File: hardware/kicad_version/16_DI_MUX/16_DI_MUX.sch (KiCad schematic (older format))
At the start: 39 parts, among them P1 CONN_2, P2 CONN_2, P3 CONN_2, P4 CONN_2, U1 74LS165

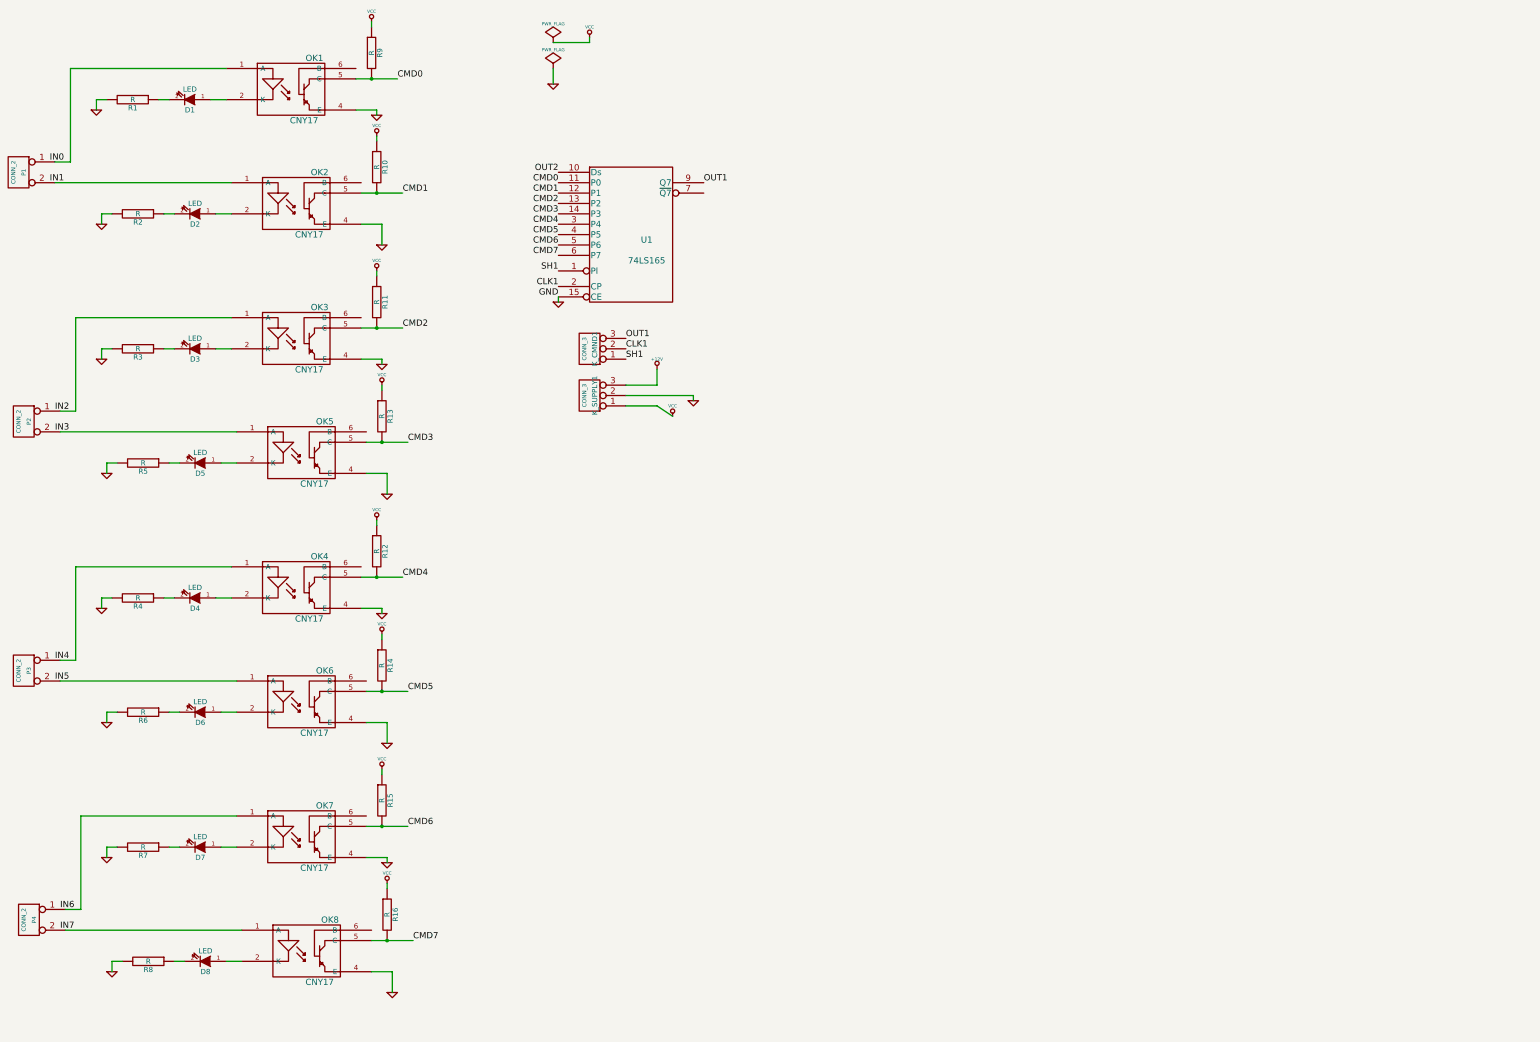
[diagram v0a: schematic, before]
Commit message: ajout de 8 entr?es correction Vcc -> 5V ajout footprint molex 2 vertical
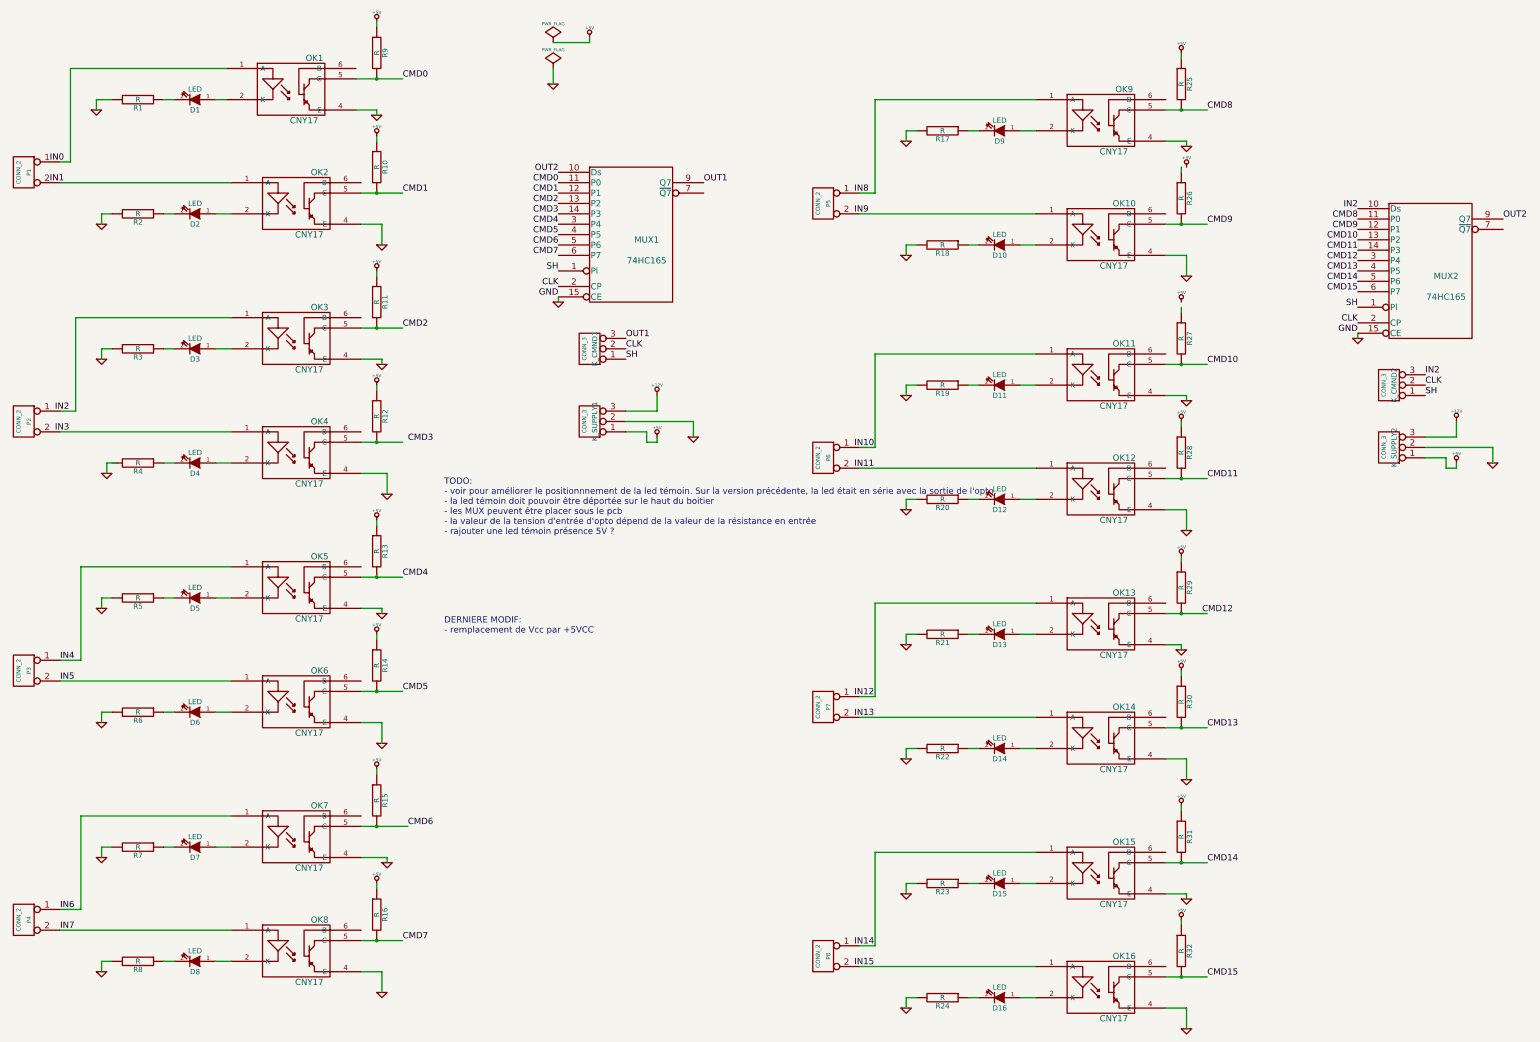
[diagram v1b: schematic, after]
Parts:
- added D10, D11, D12, D13, D14, D15, D16, D9: LED, symbol LED
- added K_CMND2, K_SUPPLY2: CONN_3, symbol CONN_3
- added MUX2: 74HC165, symbol 74LS165
- added OK10, OK11, OK12, OK13, OK14, OK15, OK16, OK9: CNY17, symbol OPTO-TRANSISTOR
- added P5, P6, P7, P8: CONN_2, symbol CONN_2
- added R17, R18, R19, R20, R21, R22, R23, R24, R25, R26, R27, R28, R29, R30, R31, R32: R, symbol R
- MUX1: renamed from U1; value 74LS165 -> 74HC165
- renumbered D5 to D4, D4 to D5, OK5 to OK4, OK4 to OK5, R13 to R12, R12 to R13, R5 to R4, R4 to R5
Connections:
- net +12V: now also K_SUPPLY2.3 (P3)
- net CMD3: no longer OK4.5 (C), R12.2
- net GND: now also K_SUPPLY2.2 (PM), MUX2.15 (CE), MUX2.8 (GND), OK10.4 (E), OK11.4 (E), OK12.4 (E), OK13.4 (E), OK14.4 (E), OK15.4 (E), OK16.4 (E), OK9.4 (E), R17.2, R18.2, R19.2, R20.2, R21.2, R22.2, R23.2, R24.2; no longer R4.2
- net IN2: now also K_CMND2.3 (P3), MUX2.10 (Ds)
- net IN4: now also OK5.1 (A), P3.1 (P1)
- net IN5: now also OK6.1 (A), P3.2 (PM)
- net IN6: now also OK7.1 (A), P4.1 (P1)
- net IN7: now also OK8.1 (A), P4.2 (PM)
- net OUT2: now also MUX2.9 (Q7)
- net VCC: now also MUX2.16 (VCC); no longer K_SUPPLY1.1 (P1), R10.1, R11.1, R12.1, R13.1, R14.1, R15.1, R16.1, R9.1
- net CLK1 renamed CLK
- net CLK: now also K_CMND2.2 (PM), MUX2.2 (CP)
- net SH1 renamed SH
- net SH: now also K_CMND2.1 (P1), MUX2.1 (Pl)
- new net: OK4.5 (C), R12.2
- new net: OK13.1 (A), P7.1 (P1)
- new net: D13.1 (A), OK13.2 (K)
- new net: D13.2 (K), R21.1
- new net: OK14.1 (A), P7.2 (PM)
- new net: D14.1 (A), OK14.2 (K)
- new net: D14.2 (K), R22.1
- new net: OK16.1 (A), P8.2 (PM)
- new net: D16.1 (A), OK16.2 (K)
- new net: D16.2 (K), R24.1
- new net: OK15.1 (A), P8.1 (P1)
- new net: D15.1 (A), OK15.2 (K)
- new net: D15.2 (K), R23.1
- new net: OK11.1 (A), P6.1 (P1)
- new net: D11.1 (A), OK11.2 (K)
- new net: D11.2 (K), R19.1
- new net: OK12.1 (A), P6.2 (PM)
- new net: D12.1 (A), OK12.2 (K)
- new net: D12.2 (K), R20.1
- new net: OK10.1 (A), P5.2 (PM)
- new net: D10.1 (A), OK10.2 (K)
- new net: D10.2 (K), R18.1
- new net: OK9.1 (A), P5.1 (P1)
- new net: D9.1 (A), OK9.2 (K)
- new net: D9.2 (K), R17.1
- new net +5V: K_SUPPLY1.1 (P1), K_SUPPLY2.1 (P1), R10.1, R11.1, R12.1, R13.1, R14.1, R15.1, R16.1, R25.1, R28.1, R29.1, R30.1, R31.1, R32.1, R9.1
- new net CMD10: MUX2.13 (P2), OK11.5 (C), R27.2
- new net CMD11: MUX2.14 (P3), OK12.5 (C), R28.2
- new net CMD12: MUX2.3 (P4), OK13.5 (C), R29.2
- new net CMD13: MUX2.4 (P5), OK14.5 (C), R30.2
- new net CMD14: MUX2.5 (P6), OK15.5 (C), R31.2
- new net CMD15: MUX2.6 (P7), OK16.5 (C), R32.2
- new net CMD8: MUX2.11 (P0), OK9.5 (C), R25.2
- new net CMD9: MUX2.12 (P1), OK10.5 (C), R26.2
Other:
- note added: "DERNIERE MODIF:\n- remplacement de Vcc par +5VCC"
- note added: "TODO:\n- voir pour améliorer le positionnnement de la led témoin. Sur la version précédente, la led était en série avec la sortie de l'opto.\n- la led témoin doit pouvoir être déportée sur le haut du boitier\n- les MUX peuvent être placer sous le pcb\n- la valeur de la tension d'entrée d'opto dépend de la valeur de la résistance en entrée\n- rajouter une led témoin présence 5V ?"
- moved on the sheet: D1, D4, D6, D7, D8, K_SUPPLY1, OK4, OK6, OK7, OK8, P1, P4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

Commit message: diverse petites corrections du schema essais de routage
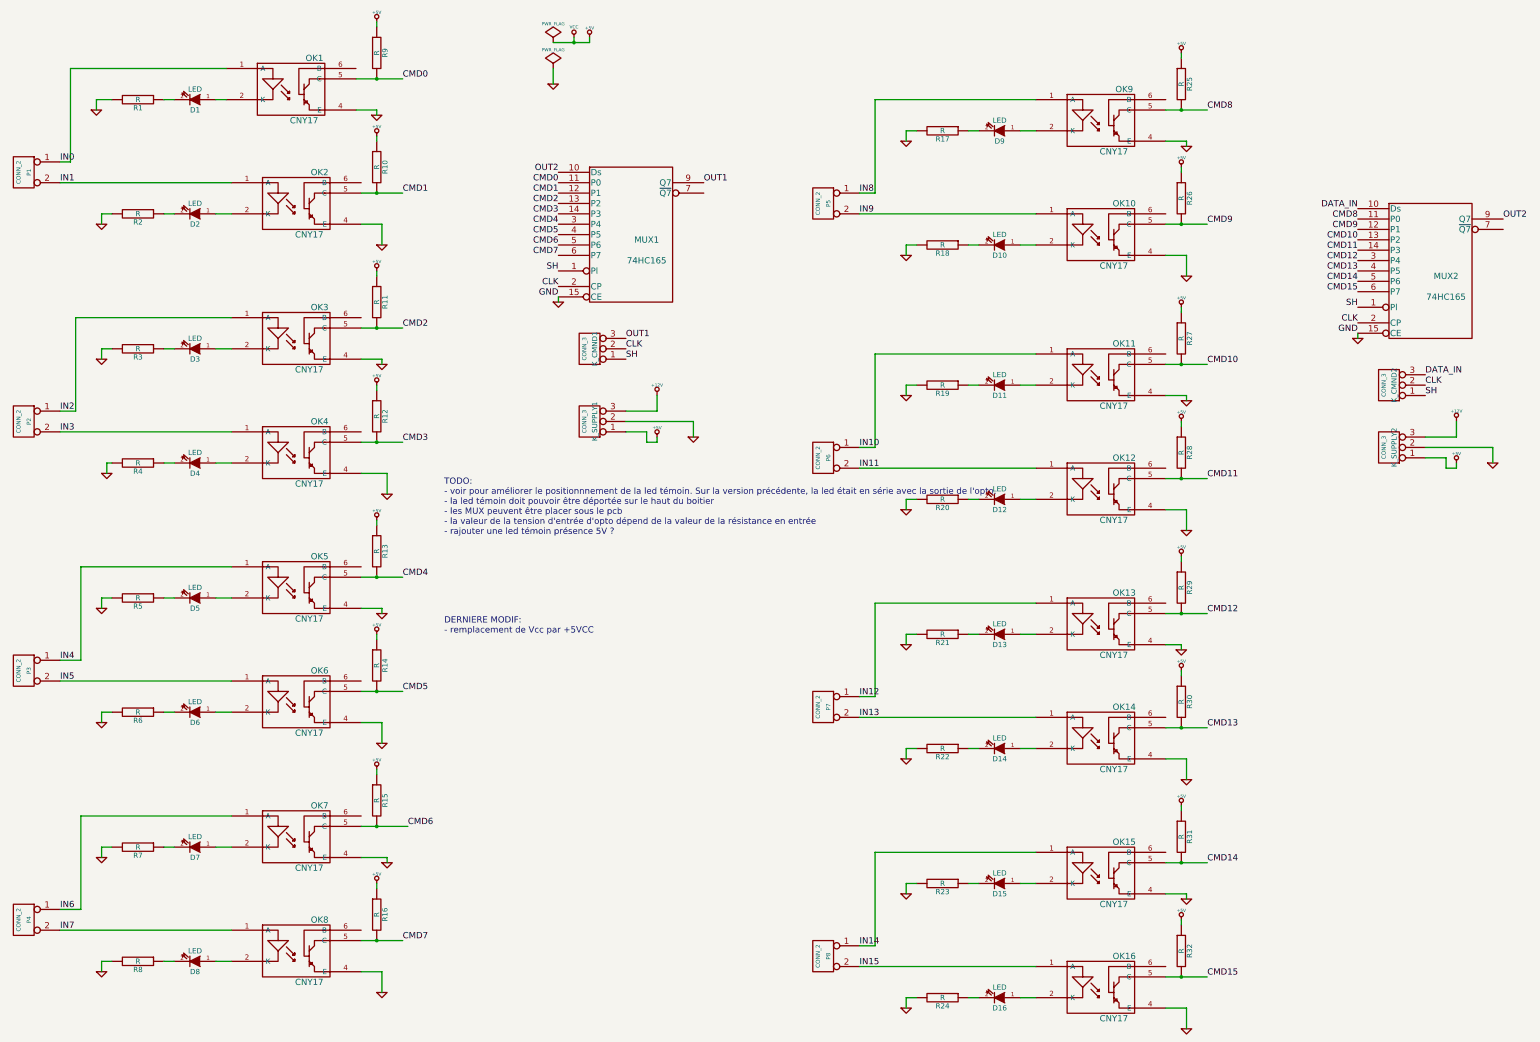
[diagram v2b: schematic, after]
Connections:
- net VCC is gone; now on net +5V: MUX1.16 (VCC), MUX2.16 (VCC)
- net +5V: now also R26.1, R27.1
- net CMD3: now also OK4.5 (C), R12.2
- net GND: now also R4.2
- net IN0: now also OK1.1 (A), P1.1 (P1)
- net IN1: now also OK2.1 (A), P1.2 (PM)
- net IN10: now also OK11.1 (A), P6.1 (P1)
- net IN11: now also OK12.1 (A), P6.2 (PM)
- net IN12: now also OK13.1 (A), P7.1 (P1)
- net IN13: now also OK14.1 (A), P7.2 (PM)
- net IN14: now also OK15.1 (A), P8.1 (P1)
- net IN15: now also OK16.1 (A), P8.2 (PM)
- net IN2: now also OK3.1 (A), P2.1 (P1); no longer K_CMND2.3 (P3), MUX2.10 (Ds)
- net IN3: now also OK4.1 (A), P2.2 (PM)
- net IN8: now also OK9.1 (A), P5.1 (P1)
- net IN9: now also OK10.1 (A), P5.2 (PM)
- new net DATA_IN: K_CMND2.3 (P3), MUX2.10 (Ds)
